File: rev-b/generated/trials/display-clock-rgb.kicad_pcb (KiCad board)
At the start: 4 copper layers, 136 x 106 mm, 351 parts, among them J1001 LCD RGB / contact fit pending, J1002 CAP TOUCH / contact fit pendi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, J1101 FOOT WIRE: 1SIGNAL 2GND, J1102 FOOT WIRE: 1SIGNAL 2GND, J201 NMJ4HCD2 INPUT, J202 NMJ4HCD2 OUTPUT, J401 PJ-102AH, J501 GOWIN JTAG / target VREF only, J701 UART / POWERED TARGET ONLY, Q401 AO4407A, SW501 RECONFIG / MPN pending, SW701 RESET / SMD button MPN pending, SW702 BOOT / SMD button MPN pending, U101 TPS54302DDCR, U102 TPS54302DDCR, U1101 SN74LVC1G17DCKR, U1102 SN74LVC1G17DCKR, U201 PCM1808PWR, U202 PCM5102APWR, U203 OPA1656IDR, U204 TLV76750DRVR, U205 TLV75533PDBVR, U206 TPS3808G01DBVR, U207 TPS3808G01DBVR, U301 TLV62569DBVR, U302 TPS3897ADRYR, U303 TPS22965DSGR, U501 GW2AR-LV18QN88C8/I7, U502 GD25Q32ESIGR, U503 SN74LVC1G125DCKR, U504 SN74LVC1G17DCKR, U601 TLV62569DBVR, U701 ESP32-P4NRW16X, U702 GD25Q32ESIGR, U801 SN74AXC4T774PWR, U802 TPS3808G01DBVR, U803 SN74LVC1G00DCKR, U901 TPS61169DCKR, U902 SN74LVC1G125DCKR, U903 TLV76701DRVR, U904 TLV76701DRVR, Y501 24.576MHz / 3.3V CMOS XO / MP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, Y701 40MHz / +/-10ppm / MPN and CL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

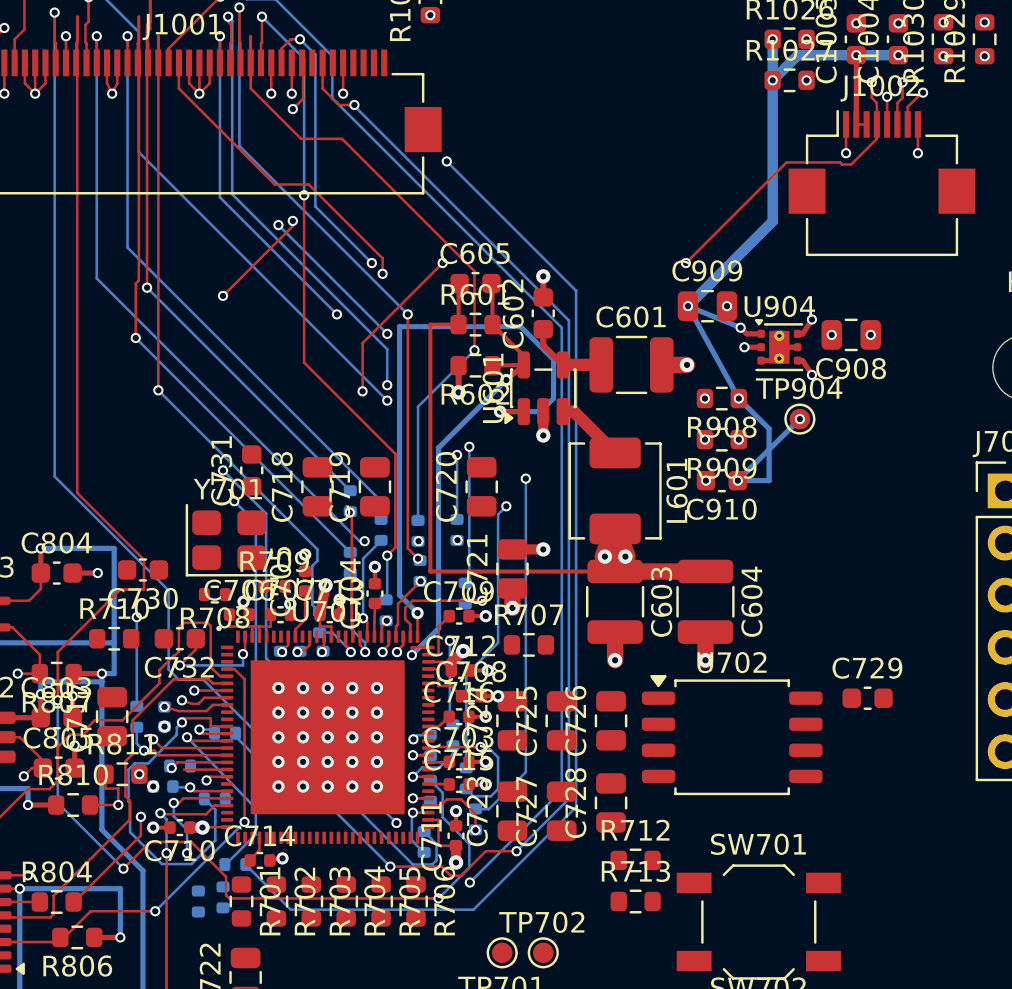
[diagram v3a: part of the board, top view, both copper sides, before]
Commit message: Route touch SDA with coordinated VSYNC and SDA resistor poses
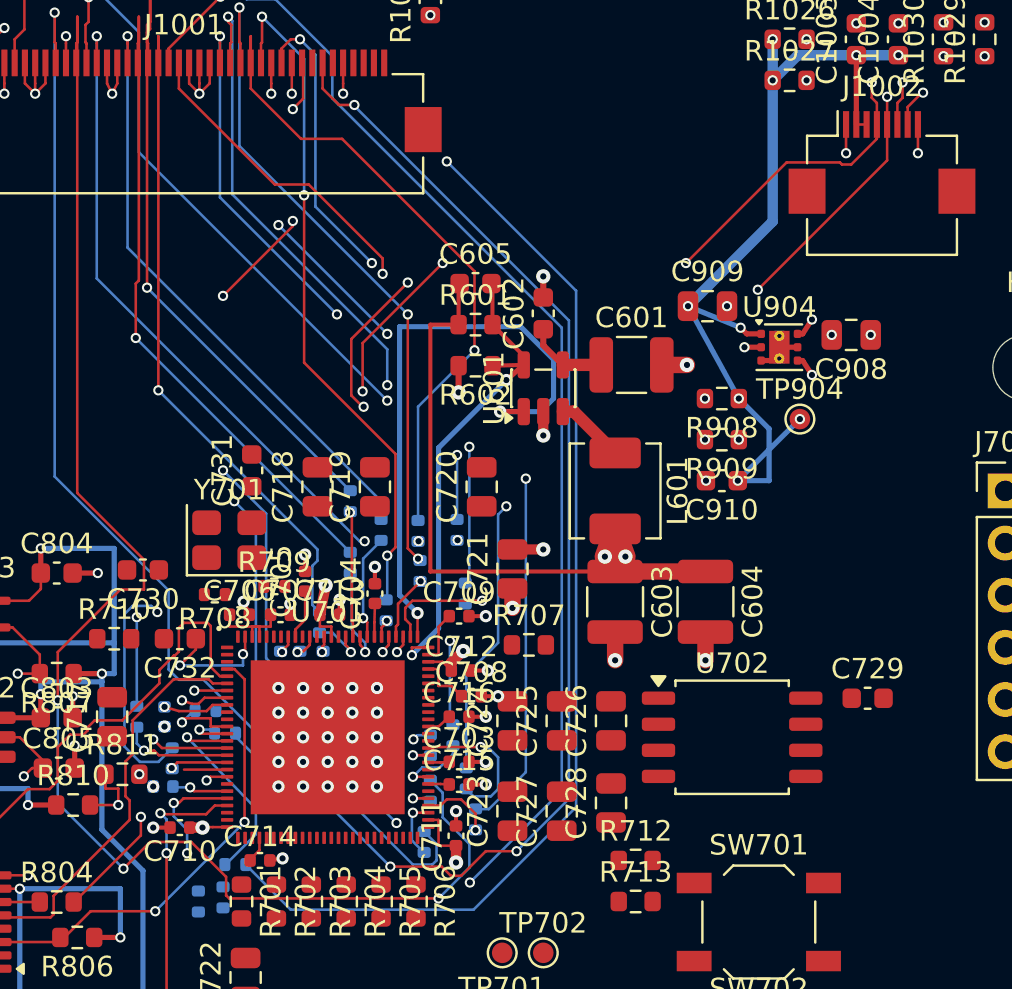
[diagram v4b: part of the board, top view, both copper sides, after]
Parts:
- R1019, R1023: footprint Resistor_SMD:R_0402_1005Metric -> KestrelTiming:R_0402_1005Metric_Courtyard0p10
- moved R1019 4.32 mm to (118.0, 84.7)
- moved R1023 0.54 mm to (116.4, 87.0), turned to 90 degrees
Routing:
- net /RGB565 and capacitive touch/TOUCH_SDA: track 5.36 -> 66.2 mm, vias 2 -> 6
- net /MCU_LCD_VSYNC: track 17.2 -> 3.63 mm
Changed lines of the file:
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@@
 		)
 	)
-	(footprint "Resistor_SMD:R_0402_1005Metric"
+	(footprint "KestrelTiming:R_0402_1005Metric_Courtyard0p10"
 		(layer "B.Cu")
-		(at 118.5 89)
+		(at 118.05 84.7)
 		(descr "Resistor SMD 0402 (1005 Metric), square (rectangular) end terminal, IPC-7351 nominal, (Body size source: IPC-SM-782 page 72, https://www.pcb-3d.com/wordpress/wp-content/uploads/ipc-sm-782a_amendment_1_and_2.pdf)")
 		(tags "resistor")
@@
 		)
 		(fp_rect
-			(start -0.93 0.47)
-			(end 0.93 -0.47)
+			(start -0.88 -0.42)
+			(end 0.88 0.42)
 			(stroke
 				(width 0.05)
@@
 		)
 	)
-	(footprint "Resistor_SMD:R_0402_1005Metric"
+	(footprint "KestrelTiming:R_0402_1005Metric_Courtyard0p10"
 		(layer "B.Cu")
-		(at 116.81 87.4)
+		(at 116.425 87.025 90)
 		(descr "Resistor SMD 0402 (1005 Metric), square (rectangular) end terminal, IPC-7351 nominal, (Body size source: IPC-SM-782 page 72, https://www.pcb-3d.com/wordpress/wp-content/uploads/ipc-sm-782a_amendment_1_and_2.pdf)")
 		(tags "resistor")
 		(property "Reference" "R1023"
-			(at 0 1.17 180)
+			(at 0 1.17 270)
 			(layer "B.SilkS")
 			(effects
@@
 		)
 		(property "Value" "33ohm"
-			(at 0 -1.17 180)
+			(at 0 -1.17 270)
 			(layer "B.Fab")
 			(effects
@@
 		)
 		(property "Datasheet" "https://www.yageogroup.com/component-documentation/download/specsheet/RC0402FR-0733RL"
-			(at 0 0 180)
+			(at 0 0 270)
 			(layer "B.Fab")
 			(hide yes)
@@
 		)
 		(property "Description" ""
-			(at 0 0 180)
+			(at 0 0 270)
 			(layer "B.Fab")
 			(hide yes)
@@
 		)
 		(property "KiLib_Generator" "SMD_2terminal_chip_molded"
-			(at 0 0 180)
+			(at 0 0 270)
 			(layer "B.SilkS")
 			(hide yes)
@@
 		)
 		(property "Manufacturer" "YAGEO"
-			(at 0 0 180)
+			(at 0 0 270)
 			(layer "B.SilkS")
 			(hide yes)
@@
 		)
 		(property "MPN" "RC0402FR-0733RL"
-			(at 0 0 180)
+			(at 0 0 270)
 			(layer "B.SilkS")
 			(hide yes)
@@
 		)
 		(property "LCSC" "C138002"
-			(at 0 0 180)
+			(at 0 0 270)
 			(layer "B.SilkS")
 			(hide yes)
@@
 		)
 		(property "Rating" "33ohm / 1% / 0.063W at 70C / 50V limiting voltage / GPIO source damping starting value"
-			(at 0 0 180)
+			(at 0 0 270)
 			(layer "B.SilkS")
 			(hide yes)
@@
 		)
 		(property "AssemblySide" "B.Cu / source damping passives; assembly qualification pending"
-			(at 0 0 270)
+			(at 0 0 0)
 			(layer "B.SilkS")
 			(hide yes)
@@
 		)
 		(fp_rect
-			(start -0.93 0.47)
-			(end 0.93 -0.47)
+			(start 0.88 -0.42)
+			(end -0.88 0.42)
 			(stroke
 				(width 0.05)
@@
 		)
 		(fp_text user "${REFERENCE}"
-			(at 0 0 180)
+			(at 0 0 270)
 			(layer "B.Fab")
 			(effects
@@
 		)
 		(pad "1" smd roundrect
-			(at -0.51 0)
+			(at -0.51 0 90)
 			(size 0.54 0.64)
 			(layers "B.Cu" "B.Mask" "B.Paste")
@@
 		)
 		(pad "2" smd roundrect
-			(at 0.51 0)
+			(at 0.51 0 90)
 			(size 0.54 0.64)
 			(layers "B.Cu" "B.Mask" "B.Paste")
@@
 		(net "/RGB565 and capacitive touch/TOUCH_SDA")
 	)
+	(segment
+		(start 151.25 57.9)
+		(end 151.25 56.15)
+		(width 0.127)
+		(layer "F.Cu")
+		(net "/RGB565 and capacitive touch/TOUCH_SDA")
+	)
+	(segment
+		(start 125.15 69.35)
+		(end 125.15 66.599999)
+		(width 0.127)
+		(layer "F.Cu")
+		(net "/RGB565 and capacitive touch/TOUCH_SDA")
+	)
+	(segment
+		(start 144.95 64.2)
+		(end 151.25 57.9)
+		(width 0.127)
+		(layer "F.Cu")
+		(net "/RGB565 and capacitive touch/TOUCH_SDA")
+	)
+	(segment
+		(start 125.7 69.9)
+		(end 125.15 69.35)
+		(width 0.127)
+		(layer "F.Cu")
+		(net "/RGB565 and capacitive touch/TOUCH_SDA")
+	)
+	(segment
+		(start 125.15 66.599999)
+		(end 127.9 63.85)
+		(width 0.127)
+		(layer "F.Cu")
+		(net "/RGB565 and capacitive touch/TOUCH_SDA")
+	)
+	(segment
+		(start 125.75 69.9)
+		(end 125.7 69.9)
+		(width 0.127)
+		(layer "F.Cu")
+		(net "/RGB565 and capacitive touch/TOUCH_SDA")
+	)
+	(via
+		(at 125.75 69.9)
+		(size 0.5)
+		(drill 0.3)
+		(layers "F.Cu" "B.Cu")
+		(net "/RGB565 and capacitive touch/TOUCH_SDA")
+	)
+	(via
+		(at 144.95 64.2)
+		(size 0.5)
+		(drill 0.3)
+		(layers "F.Cu" "B.Cu")
+		(net "/RGB565 and capacitive touch/TOUCH_SDA")
+	)
+	(via
+		(at 115.7 79.9)
+		(size 0.5)
+		(drill 0.3)
+		(layers "F.Cu" "B.Cu")
+		(net "/RGB565 and capacitive touch/TOUCH_SDA")
+	)
 	(via
 		(at 151.25 54.8)
@@
 		(net "/RGB565 and capacitive touch/TOUCH_SDA")
 	)
+	(via
+		(at 127.9 63.85)
+		(size 0.5)
+		(drill 0.3)
+		(layers "F.Cu" "B.Cu")
+		(net "/RGB565 and capacitive touch/TOUCH_SDA")
+	)
+	(segment
+		(start 116.425 86.515)
+		(end 116.45 86.5)
+		(width 0.127)
+		(layer "B.Cu")
+		(net "/RGB565 and capacitive touch/TOUCH_SDA")
+	)
+	(segment
+		(start 114.1 86.45)
+		(end 114.1 80)
+		(width 0.127)
+		(layer "B.Cu")
+		(net "/RGB565 and capacitive touch/TOUCH_SDA")
+	)
+	(segment
+		(start 114.1 80)
+		(end 114.5 79.6)
+		(width 0.127)
+		(layer "B.Cu")
+		(net "/RGB565 and capacitive touch/TOUCH_SDA")
+	)
+	(segment
+		(start 115.4 79.6)
+		(end 115.7 79.9)
+		(width 0.127)
+		(layer "B.Cu")
+		(net "/RGB565 and capacitive touch/TOUCH_SDA")
+	)
+	(segment
+		(start 115.75 87.2)
+		(end 114.85 87.2)
+		(width 0.127)
+		(layer "B.Cu")
+		(net "/RGB565 and capacitive touch/TOUCH_SDA")
+	)
+	(segment
+		(start 116.45 86.5)
+		(end 115.75 87.2)
+		(width 0.127)
+		(layer "B.Cu")
+		(net "/RGB565 and capacitive touch/TOUCH_SDA")
+	)
+	(segment
+		(start 114.85 87.2)
+		(end 114.1 86.45)
+		(width 0.127)
+		(layer "B.Cu")
+		(net "/RGB565 and capacitive touch/TOUCH_SDA")
+	)
+	(segment
+		(start 114.5 79.6)
+		(end 115.4 79.6)
+		(width 0.127)
+		(layer "B.Cu")
+		(net "/RGB565 and capacitive touch/TOUCH_SDA")
+	)
+	(segment
+		(start 125.7 69.9)
+		(end 125.75 69.9)
+		(width 0.127)
+		(layer "In2.Cu")
+		(net "/RGB565 and capacitive touch/TOUCH_SDA")
+	)
+	(segment
+		(start 115.7 79.9)
+		(end 125.7 69.9)
+		(width 0.127)
+		(layer "In2.Cu")
+		(net "/RGB565 and capacitive touch/TOUCH_SDA")
+	)
+	(segment
+		(start 128.25 64.2)
+		(end 144.95 64.2)
+		(width 0.127)
+		(layer "In2.Cu")
+		(net "/RGB565 and capacitive touch/TOUCH_SDA")
+	)
 	(segment
 		(start 151.25 54.8)
@@
 	)
 	(segment
+		(start 127.9 63.85)
+		(end 128.25 64.2)
+		(width 0.127)
+		(layer "In2.Cu")
+		(net "/RGB565 and capacitive touch/TOUCH_SDA")
+	)
+	(segment
 		(start 58.325 67.099999)
 		(end 58.35 67.099999)
@@
 	)
 	(segment
-		(start 114.375 89.2)
-		(end 114.375 90.625)
-		(width 0.127)
-		(layer "B.Cu")
-		(net "/MCU_LCD_VSYNC")
-	)
-	(segment
-		(start 116.65 85.525)
-		(end 116.65 85.825)
-		(width 0.127)
-		(layer "B.Cu")
-		(net "/MCU_LCD_VSYNC")
-	)
-	(segment
-		(start 116.625 85.9)
-		(end 115.25 87.275)
-		(width 0.127)
-		(layer "B.Cu")
-		(net "/MCU_LCD_VSYNC")
-	)
-	(segment
-		(start 116.65 85.825)
-		(end 116.625 85.85)
-		(width 0.127)
-		(layer "B.Cu")
-		(net "/MCU_LCD_VSYNC")
-	)
-	(segment
-		(start 115.25 87.275)
-		(end 114.6 87.275)
-		(width 0.127)
-		(layer "B.Cu")
-		(net "/MCU_LCD_VSYNC")
-	)
-	(segment
-		(start 118.525 91.025)
-		(end 118.525 89.525)
-		(width 0.127)
-		(layer "B.Cu")
-		(net "/MCU_LCD_VSYNC")
-	)
-	(segment
-		(start 114.6 87.275)
-		(end 114.3 87.575)
-		(width 0.127)
-		(layer "B.Cu")
-		(net "/MCU_LCD_VSYNC")
-	)
-	(segment
-		(start 114.3 87.575)
-		(end 114.3 89.125)
-		(width 0.127)
-		(layer "B.Cu")
-		(net "/MCU_LCD_VSYNC")
-	)
-	(segment
-		(start 118 89)
-		(end 117.99 89)
-		(width 0.127)
-		(layer "B.Cu")
-		(net "/MCU_LCD_VSYNC")
-	)
-	(segment
-		(start 114.3 89.125)
-		(end 114.375 89.2)
-		(width 0.127)
-		(layer "B.Cu")
-		(net "/MCU_LCD_VSYNC")
-	)
-	(segment
-		(start 115.925 92.175)
-		(end 117.375 92.175)
-		(width 0.127)
-		(layer "B.Cu")
-		(net "/MCU_LCD_VSYNC")
-	)
-	(segment
-		(start 117.375 92.175)
-		(end 118.525 91.025)
-		(width 0.127)
-		(layer "B.Cu")
-		(net "/MCU_LCD_VSYNC")
-	)
-	(segment
-		(start 118.525 89.525)
-		(end 118 89)
-		(width 0.127)
-		(layer "B.Cu")
-		(net "/MCU_LCD_VSYNC")
-	)
-	(segment
-		(start 114.375 90.625)
-		(end 115.925 92.175)
+		(start 117.475 84.7)
+		(end 117.49 84.7)
 		(width 0.127)
 		(layer "B.Cu")
@@
 	(segment
 		(start 116.9 85.275)
-		(end 116.65 85.525)
-		(width 0.127)
-		(layer "B.Cu")
-		(net "/MCU_LCD_VSYNC")
-	)
-	(segment
-		(start 116.625 85.85)
-		(end 116.625 85.9)
+		(end 117.475 84.7)
 		(width 0.127)
 		(layer "B.Cu")

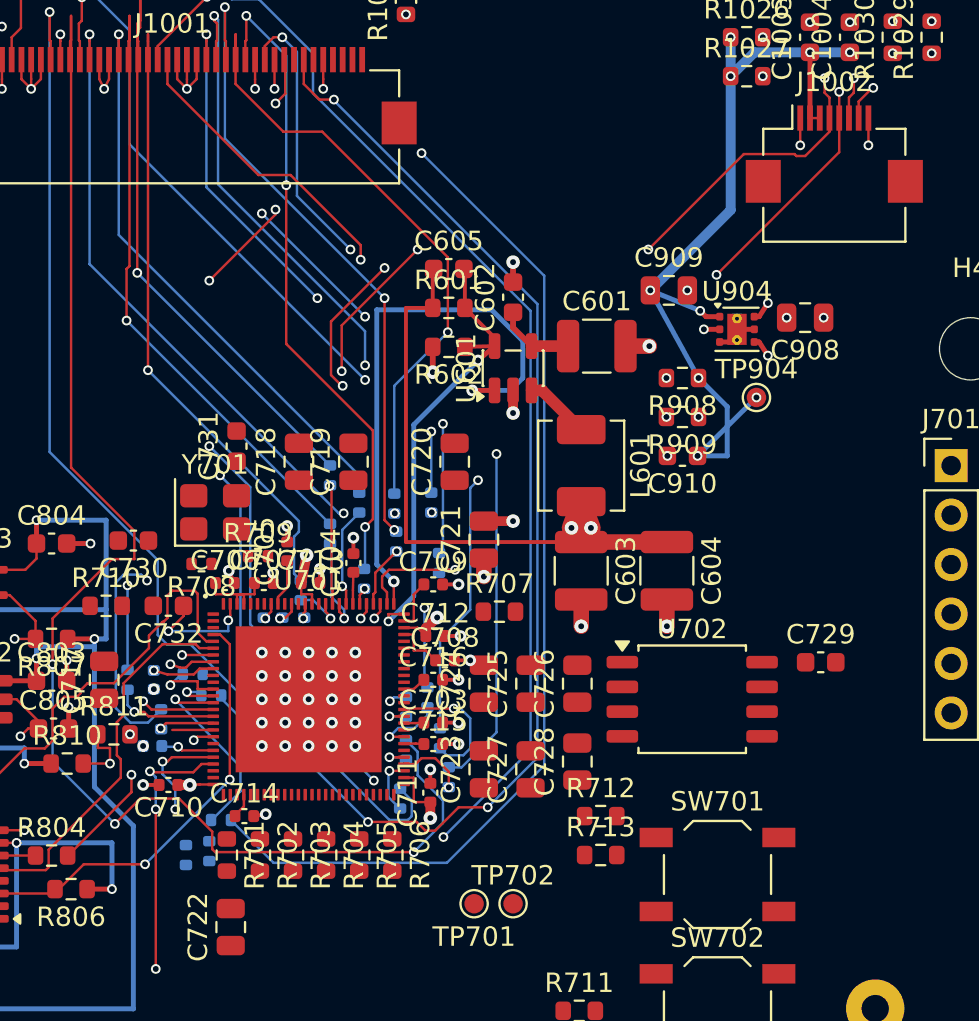
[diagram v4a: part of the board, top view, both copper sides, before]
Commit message: Complete touch reset source and output in guarded display trial
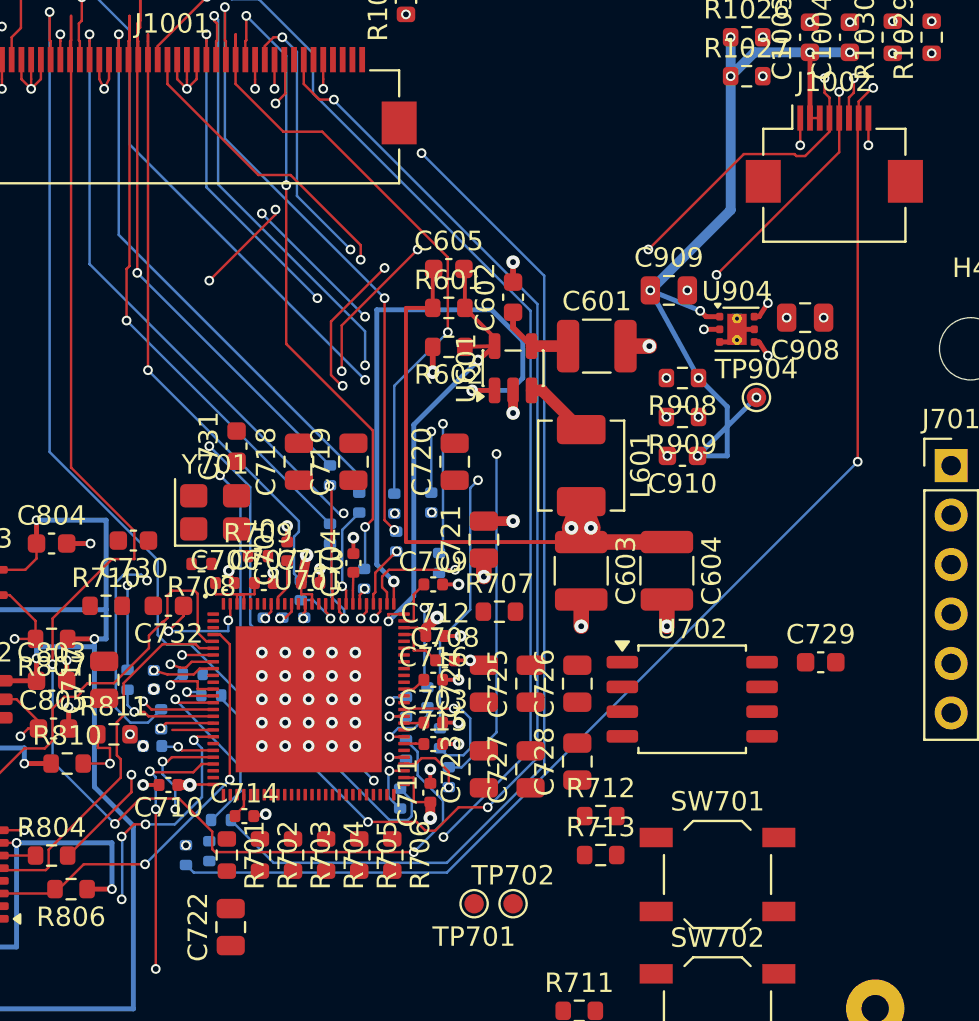
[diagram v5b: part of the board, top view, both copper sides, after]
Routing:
- net /RGB565 and capacitive touch/TOUCH_RST_N: track 5.38 -> 66.5 mm, vias 2 -> 3
- net /MCU_TOUCH_RST_N: track 1.07 -> 16.8 mm, vias 1 -> 5
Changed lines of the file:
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@@
 	)
 	(segment
+		(start 152.2 73.8)
+		(end 152.2 56.2)
+		(width 0.127)
+		(layer "F.Cu")
+		(net "/RGB565 and capacitive touch/TOUCH_RST_N")
+	)
+	(segment
 		(start 152.25 55.3)
 		(end 152.95 54.6)
@@
 		(net "/RGB565 and capacitive touch/TOUCH_RST_N")
 	)
+	(segment
+		(start 152.2 56.2)
+		(end 152.25 56.15)
+		(width 0.127)
+		(layer "F.Cu")
+		(net "/RGB565 and capacitive touch/TOUCH_RST_N")
+	)
+	(via
+		(at 152.2 73.8)
+		(size 0.5)
+		(drill 0.3)
+		(layers "F.Cu" "B.Cu")
+		(net "/RGB565 and capacitive touch/TOUCH_RST_N")
+	)
 	(via
 		(at 156 52.825)
@@
 	)
 	(segment
+		(start 131.1 94.9)
+		(end 152.2 73.8)
+		(width 0.127)
+		(layer "B.Cu")
+		(net "/RGB565 and capacitive touch/TOUCH_RST_N")
+	)
+	(segment
+		(start 117.7 94.51)
+		(end 117.7 94.5)
+		(width 0.127)
+		(layer "B.Cu")
+		(net "/RGB565 and capacitive touch/TOUCH_RST_N")
+	)
+	(segment
+		(start 118.1 94.9)
+		(end 131.1 94.9)
+		(width 0.127)
+		(layer "B.Cu")
+		(net "/RGB565 and capacitive touch/TOUCH_RST_N")
+	)
+	(segment
+		(start 117.7 94.5)
+		(end 118.1 94.9)
+		(width 0.127)
+		(layer "B.Cu")
+		(net "/RGB565 and capacitive touch/TOUCH_RST_N")
+	)
+	(segment
 		(start 153 54.6)
 		(end 156 52.825)
@@
 		(net "/MCU_TOUCH_RST_N")
 	)
+	(segment
+		(start 115.625 92.425)
+		(end 115.025 92.425)
+		(width 0.127)
+		(layer "F.Cu")
+		(net "/MCU_TOUCH_RST_N")
+	)
+	(segment
+		(start 115.025 92.425)
+		(end 114.4 93.05)
+		(width 0.127)
+		(layer "F.Cu")
+		(net "/MCU_TOUCH_RST_N")
+	)
+	(via
+		(at 117.7 93.5)
+		(size 0.5)
+		(drill 0.3)
+		(layers "F.Cu" "B.Cu")
+		(net "/MCU_TOUCH_RST_N")
+	)
+	(via
+		(at 114.4 96.275)
+		(size 0.5)
+		(drill 0.3)
+		(layers "F.Cu" "B.Cu")
+		(net "/MCU_TOUCH_RST_N")
+	)
+	(via
+		(at 115.625 92.425)
+		(size 0.5)
+		(drill 0.3)
+		(layers "F.Cu" "B.Cu")
+		(net "/MCU_TOUCH_RST_N")
+	)
+	(via
+		(at 114.4 93.05)
+		(size 0.5)
+		(drill 0.3)
+		(layers "F.Cu" "B.Cu")
+		(net "/MCU_TOUCH_RST_N")
+	)
 	(via
 		(at 118.1 88.1)
@@
 		(net "/MCU_TOUCH_RST_N")
 	)
+	(segment
+		(start 118.1 88.1)
+		(end 118.525 88.525)
+		(width 0.127)
+		(layer "B.Cu")
+		(net "/MCU_TOUCH_RST_N")
+	)
+	(segment
+		(start 114.425 93.075)
+		(end 114.425 96.25)
+		(width 0.127)
+		(layer "B.Cu")
+		(net "/MCU_TOUCH_RST_N")
+	)
+	(segment
+		(start 117.125 92.425)
+		(end 115.625 92.425)
+		(width 0.127)
+		(layer "B.Cu")
+		(net "/MCU_TOUCH_RST_N")
+	)
+	(segment
+		(start 114.425 96.25)
+		(end 114.4 96.275)
+		(width 0.127)
+		(layer "B.Cu")
+		(net "/MCU_TOUCH_RST_N")
+	)
+	(segment
+		(start 118.525 88.525)
+		(end 118.525 91.025)
+		(width 0.127)
+		(layer "B.Cu")
+		(net "/MCU_TOUCH_RST_N")
+	)
+	(segment
+		(start 117.7 93.5)
+		(end 117.7 93.49)
+		(width 0.127)
+		(layer "B.Cu")
+		(net "/MCU_TOUCH_RST_N")
+	)
+	(segment
+		(start 114.4 93.05)
+		(end 114.425 93.075)
+		(width 0.127)
+		(layer "B.Cu")
+		(net "/MCU_TOUCH_RST_N")
+	)
+	(segment
+		(start 118.525 91.025)
+		(end 117.125 92.425)
+		(width 0.127)
+		(layer "B.Cu")
+		(net "/MCU_TOUCH_RST_N")
+	)
+	(segment
+		(start 114.4 96.275)
+		(end 114.925 96.275)
+		(width 0.127)
+		(layer "In2.Cu")
+		(net "/MCU_TOUCH_RST_N")
+	)
+	(segment
+		(start 114.925 96.275)
+		(end 117.7 93.5)
+		(width 0.127)
+		(layer "In2.Cu")
+		(net "/MCU_TOUCH_RST_N")
+	)
